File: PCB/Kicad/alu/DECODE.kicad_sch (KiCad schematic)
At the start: 1 part, among them U53 74LS139

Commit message: UPDATE
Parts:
- added U54, U55, U56: 74LS32, symbol 74xx:74LS32
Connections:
- net GND: now also U54.7 (GND), U55.7 (GND), U56.7 (GND)
- net VCC: now also U54.14 (VCC), U55.14 (VCC), U56.14 (VCC)
- net ~{G_SHIFT}: now reaches U53.10 (O2)
- net ~{G_SHIFT}: now also U55.10, U55.13
- net ~{G_ARITH}: now reaches U53.11 (O1)
- net ~{G_ARITH}: now also U55.2, U55.5
- net ~{G_LOG}: now reaches U53.12 (O0)
- net ~{G_LOG}: now also U54.10, U54.13, U54.2, U54.5
- net OP3: now reaches U53.13 (A1)
- net OP2: now reaches U53.14 (A0)
- net ~{G_CTRL}: now reaches U53.9 (O3)
- net ~{G_CTRL}: now also U56.2
- net OP0: now reaches U53.2 (A0)
- net OP1: now reaches U53.3 (A1)
- net ~{S0}: now reaches U53.4 (O0)
- net ~{S0}: now also U54.1, U55.1, U55.9, U56.1
- net ~{S1}: now reaches U53.5 (O1)
- net ~{S1}: now also U54.4, U55.12, U55.4
- net ~{S2}: now reaches U53.6 (O2)
- net ~{S2}: now also U54.9
- net ~{S3}: now reaches U53.7 (O3)
- net ~{S3}: now also U54.12
- new net ~{REG_LOAD}: U56.3
- new net ~{SEL_ADD}: U55.3
- new net ~{SEL_AND}: U54.6
- new net ~{SEL_NOT}: U54.11
- new net ~{SEL_OR}: U54.3
- new net ~{SEL_SHL}: U55.8
- new net ~{SEL_SHR}: U55.11
- new net ~{SEL_SUB}: U55.6
- new net ~{SEL_XOR}: U54.8
- no-connect marks 0 -> 10
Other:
- moved on the sheet: U53A, U53B, U53C

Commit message: UPDATE
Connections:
- net ~{G_CTRL}: now also U56.5
- net ~{S1}: now also U56.4
- net ~{LOAD_B_REG}: now reaches U56.6
- net ~{REG_LOAD} renamed ~{LOAD_A_REG}
- no-connect marks 10 -> 7
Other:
- moved on the sheet: U56B
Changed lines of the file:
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@@
-	)
-	(no_connect
-		(at 177.8 77.47)
 	)
 	(no_connect
@@
 	(no_connect
 		(at 177.8 93.98)
-	)
-	(no_connect
-		(at 193.04 80.01)
-	)
-	(no_connect
-		(at 177.8 82.55)
 	)
 	(wire
@@
 		)
 	)
+	(label "~{G_CTRL}"
+		(at 105.41 177.8 180)
+		(effects
+			(font
+				(size 1.27 1.27)
+			)
+			(justify right bottom)
+		)
+	)
 	(label "~{G_SHIFT}"
 		(at 105.41 132.08 180)
@@
 			)
 			(justify left bottom)
+		)
+	)
+	(label "~{S1}"
+		(at 105.41 172.72 180)
+		(effects
+			(font
+				(size 1.27 1.27)
+			)
+			(justify right bottom)
 		)
 	)
@@
 		)
 	)
-	(hierarchical_label "~{REG_LOAD}"
+	(hierarchical_label "~{LOAD_A_REG}"
 		(shape output)
 		(at 120.65 160.02 0)
@@
 			)
 			(justify right)
+		)
+	)
+	(hierarchical_label "~{LOAD_B_REG}"
+		(shape output)
+		(at 120.65 175.26 0)
+		(effects
+			(font
+				(size 1.27 1.27)
+			)
+			(justify left)
 		)
 	)
@@
 	(symbol
 		(lib_id "74xx:74LS32")
-		(at 185.42 80.01 0)
+		(at 113.03 175.26 0)
 		(unit 2)
 		(exclude_from_sim no)
@@
 		(dnp no)
 		(property "Reference" "U56"
-			(at 185.166 71.12 0)
+			(at 112.776 166.37 0)
 			(effects
 				(font
@@
 		)
 		(property "Value" "74LS32"
-			(at 185.42 73.66 0)
+			(at 113.03 168.91 0)
 			(effects
 				(font
@@
 		)
 		(property "Footprint" ""
-			(at 185.42 80.01 0)
+			(at 113.03 175.26 0)
 			(effects
 				(font
@@
 		)
 		(property "Datasheet" "http://www.ti.com/lit/gpn/sn74LS32"
-			(at 185.42 80.01 0)
+			(at 113.03 175.26 0)
 			(effects
 				(font
@@
 		)
 		(property "Description" "Quad 2-input OR"
-			(at 185.42 80.01 0)
-			(effects
-				(font
+			(at 113.03 175.26 0)
+			(effects
+				(font

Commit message: UPDATE
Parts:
- added C62, C63, C64, C65: 10n, symbol Device:C
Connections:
- net GND: now also C62.2, C63.2, C64.2, C65.2
- net VCC: now also C62.1, C63.1, C64.1, C65.1
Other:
- moved on the sheet: U56E

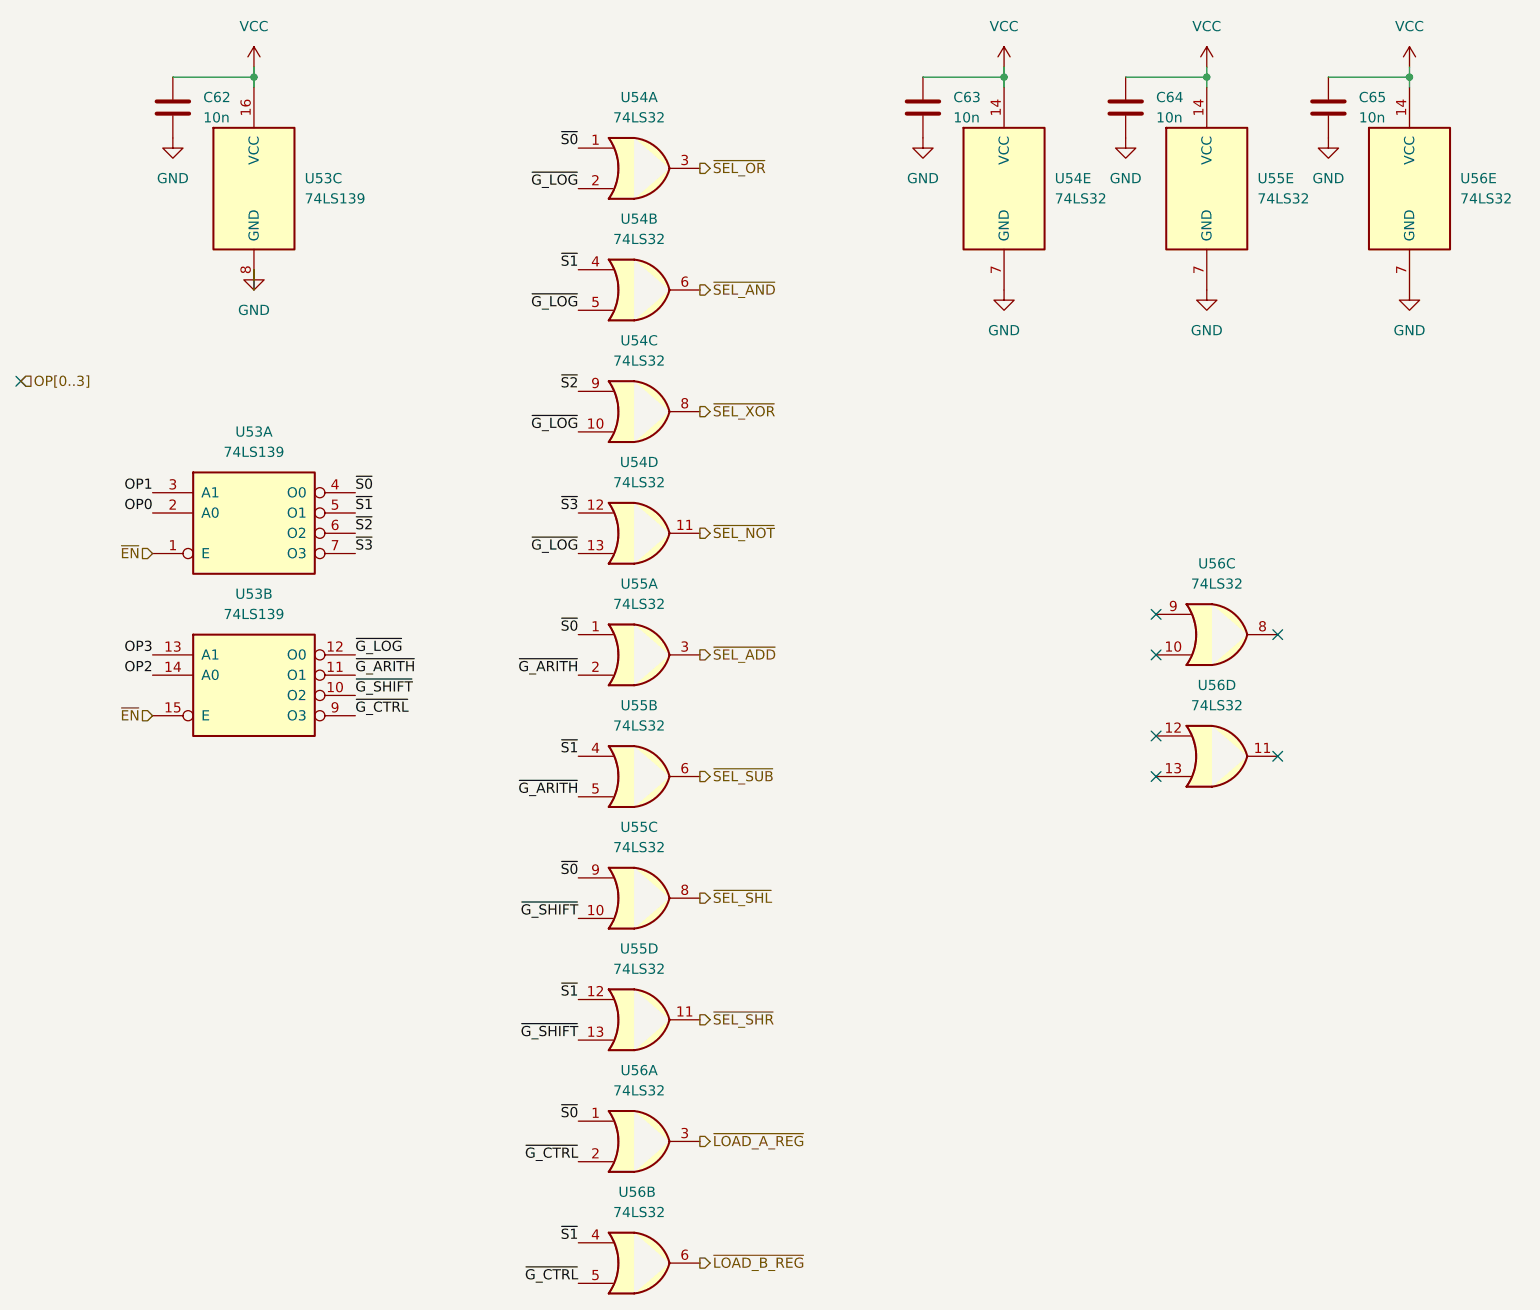
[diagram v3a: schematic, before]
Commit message: LEDs added
REGISTER.kicad_sch LEDs added to both REG_A and REG_B
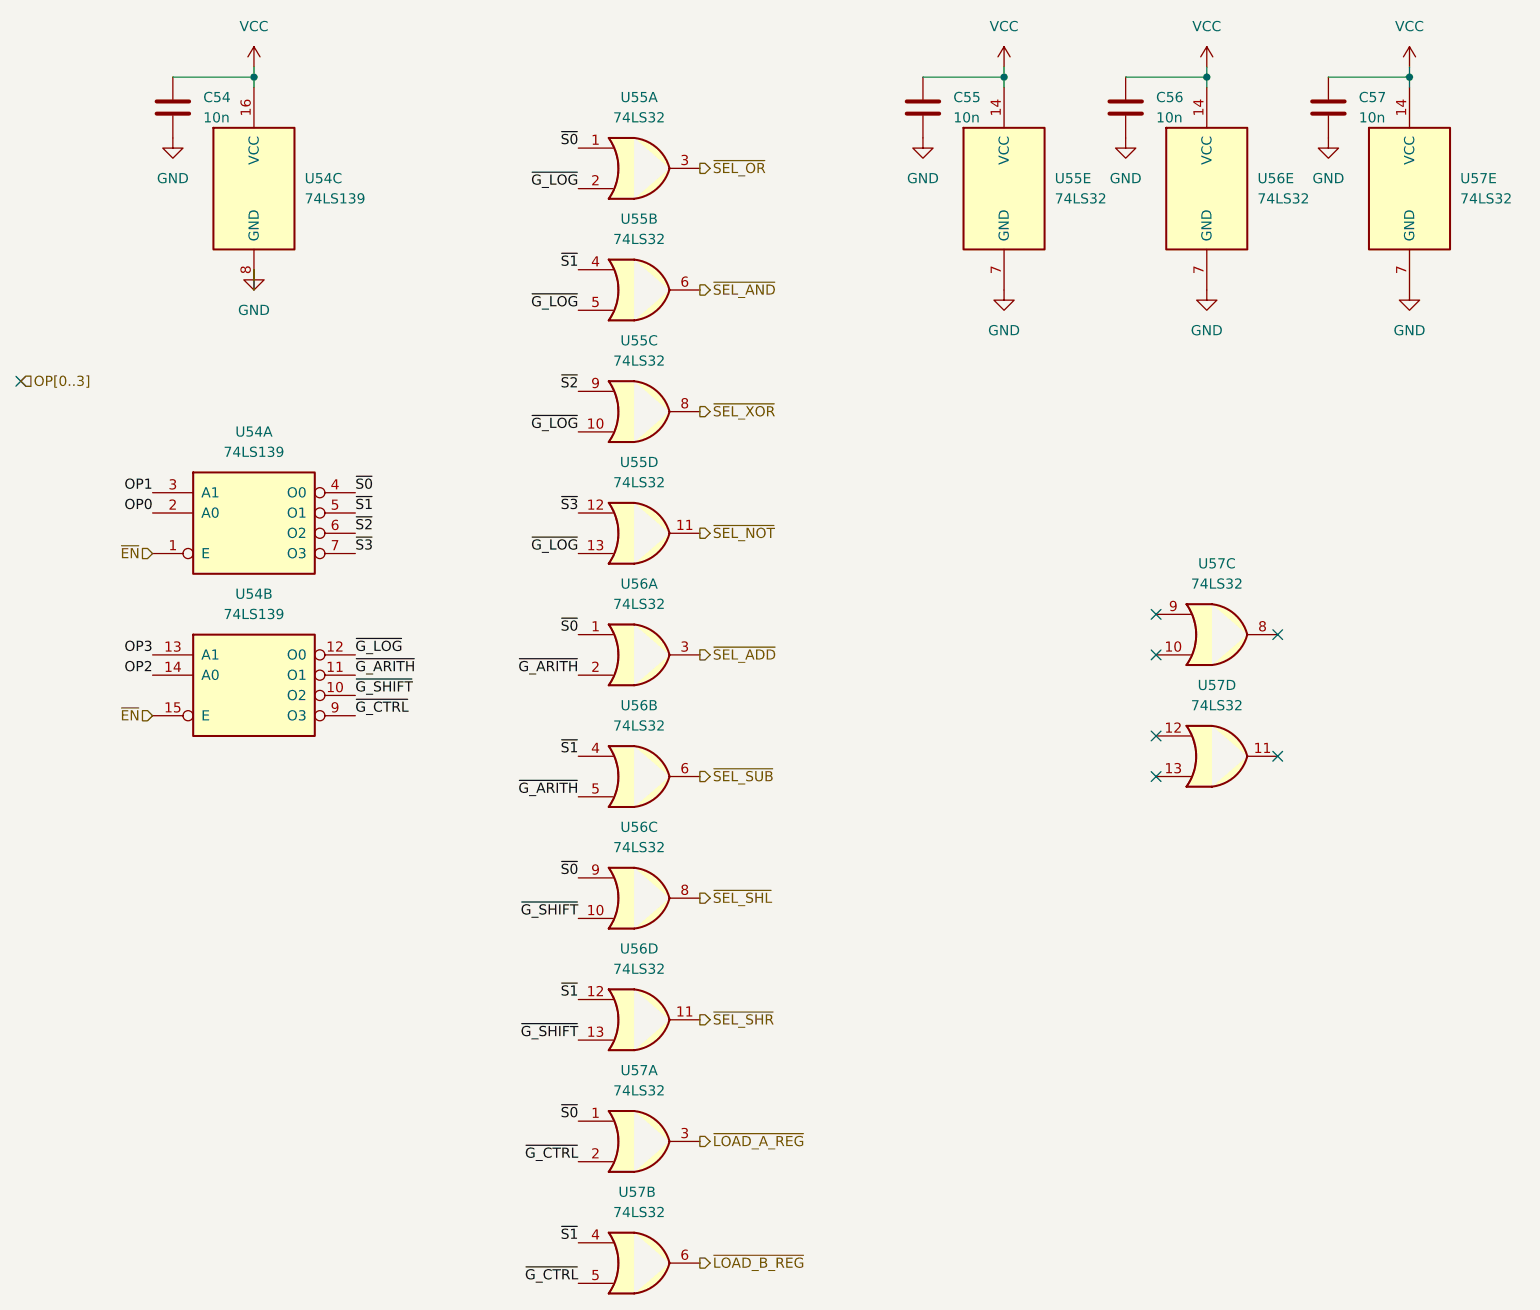
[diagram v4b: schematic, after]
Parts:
- renumbered C62 to C54, C63 to C55, C64 to C56, C65 to C57, U53 to U54, U54 to U55, U55 to U56, U56 to U57

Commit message: Footprints, PCB update
Added footprints to all components, updated the PCB with the schematic
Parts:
- C54, C55, C56, C57: footprint (none) -> Capacitor_SMD:C_0603_1608Metric
- U54: footprint (none) -> Package_SO:SOIC-16_3.9x9.9mm_P1.27mm
- U55, U56, U57: footprint (none) -> Package_SO:SOIC-14_3.9x8.7mm_P1.27mm
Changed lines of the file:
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@@
 			)
 		)
-		(property "Footprint" ""
+		(property "Footprint" "Package_SO:SOIC-14_3.9x8.7mm_P1.27mm"
 			(at 113.03 99.06 0)
 			(effects
@@
 			)
 		)
-		(property "Footprint" ""
+		(property "Footprint" "Package_SO:SOIC-14_3.9x8.7mm_P1.27mm"
 			(at 113.03 68.58 0)
 			(effects
@@
 			)
 		)
-		(property "Footprint" ""
+		(property "Footprint" "Package_SO:SOIC-14_3.9x8.7mm_P1.27mm"
 			(at 113.03 83.82 0)
 			(effects
@@
 			)
 		)
-		(property "Footprint" ""
+		(property "Footprint" "Package_SO:SOIC-14_3.9x8.7mm_P1.27mm"
 			(at 185.42 111.76 0)
 			(effects
@@
 			)
 		)
-		(property "Footprint" ""
+		(property "Footprint" "Package_SO:SOIC-14_3.9x8.7mm_P1.27mm"
 			(at 184.15 40.64 0)
 			(effects
@@
 			)
 		)
-		(property "Footprint" ""
+		(property "Footprint" "Capacitor_SMD:C_0603_1608Metric"
 			(at 200.3552 34.29 0)
 			(effects
@@
 			)
 		)
-		(property "Footprint" ""
+		(property "Footprint" "Package_SO:SOIC-14_3.9x8.7mm_P1.27mm"
 			(at 185.42 96.52 0)
 			(effects
@@
 			)
 		)
-		(property "Footprint" ""
+		(property "Footprint" "Package_SO:SOIC-14_3.9x8.7mm_P1.27mm"
 			(at 113.03 114.3 0)
 			(effects
@@
 			)
 		)
-		(property "Footprint" ""
+		(property "Footprint" "Package_SO:SOIC-14_3.9x8.7mm_P1.27mm"
 			(at 209.55 40.64 0)
 			(effects
@@
 			)
 		)
-		(property "Footprint" ""
+		(property "Footprint" "Capacitor_SMD:C_0603_1608Metric"
 			(at 55.5752 34.29 0)
 			(effects
@@
 			)
 		)
-		(property "Footprint" ""
+		(property "Footprint" "Package_SO:SOIC-14_3.9x8.7mm_P1.27mm"
 			(at 113.03 129.54 0)
 			(effects
@@
 			)
 		)
-		(property "Footprint" ""
+		(property "Footprint" "Package_SO:SOIC-16_3.9x9.9mm_P1.27mm"
 			(at 64.77 101.6 0)
 			(effects
@@
 			)
 		)
-		(property "Footprint" ""
+		(property "Footprint" "Package_SO:SOIC-14_3.9x8.7mm_P1.27mm"
 			(at 113.03 38.1 0)
 			(effects
@@
 			)
 		)
-		(property "Footprint" ""
+		(property "Footprint" "Package_SO:SOIC-16_3.9x9.9mm_P1.27mm"
 			(at 64.77 81.28 0)
 			(effects
@@
 			)
 		)
-		(property "Footprint" ""
+		(property "Footprint" "Package_SO:SOIC-14_3.9x8.7mm_P1.27mm"
 			(at 113.03 53.34 0)
 			(effects
@@
 			)
 		)
-		(property "Footprint" ""
+		(property "Footprint" "Package_SO:SOIC-14_3.9x8.7mm_P1.27mm"
 			(at 113.03 144.78 0)
 			(effects
@@
 			)
 		)
-		(property "Footprint" ""
+		(property "Footprint" "Package_SO:SOIC-14_3.9x8.7mm_P1.27mm"
 			(at 113.03 160.02 0)
 			(effects
@@
 			)
 		)
-		(property "Footprint" ""
+		(property "Footprint" "Package_SO:SOIC-14_3.9x8.7mm_P1.27mm"
 			(at 158.75 40.64 0)
 			(effects
@@
 			)
 		)
-		(property "Footprint" ""
+		(property "Footprint" "Package_SO:SOIC-14_3.9x8.7mm_P1.27mm"
 			(at 113.03 175.26 0)
 			(effects
@@
 			)
 		)
-		(property "Footprint" ""
+		(property "Footprint" "Capacitor_SMD:C_0603_1608Metric"
 			(at 174.9552 34.29 0)
 			(effects
@@
 			)
 		)
-		(property "Footprint" ""
+		(property "Footprint" "Capacitor_SMD:C_0603_1608Metric"
 			(at 149.5552 34.29 0)
 			(effects
@@
 			)
 		)
-		(property "Footprint" ""
+		(property "Footprint" "Package_SO:SOIC-16_3.9x9.9mm_P1.27mm"
 			(at 64.77 40.64 0)
 			(effects

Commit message: ALU Pcb update
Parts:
- C54, C55, C56, C57: value 10n -> 100nF; footprint Capacitor_SMD:C_0603_1608Metric -> Capacitor_SMD:C_0402_1005Metric
- U54: value 74LS139 -> 74139
- U55, U56, U57: value 74LS32 -> 7432; footprint Package_SO:SOIC-14_3.9x8.7mm_P1.27mm -> Package_SO:SO-14_3.9x8.65mm_P1.27mm
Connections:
- net VCC: now also U57.10, U57.12, U57.13, U57.9
- no-connect marks 7 -> 3
